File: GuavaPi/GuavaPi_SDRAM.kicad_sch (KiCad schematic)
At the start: 1 part

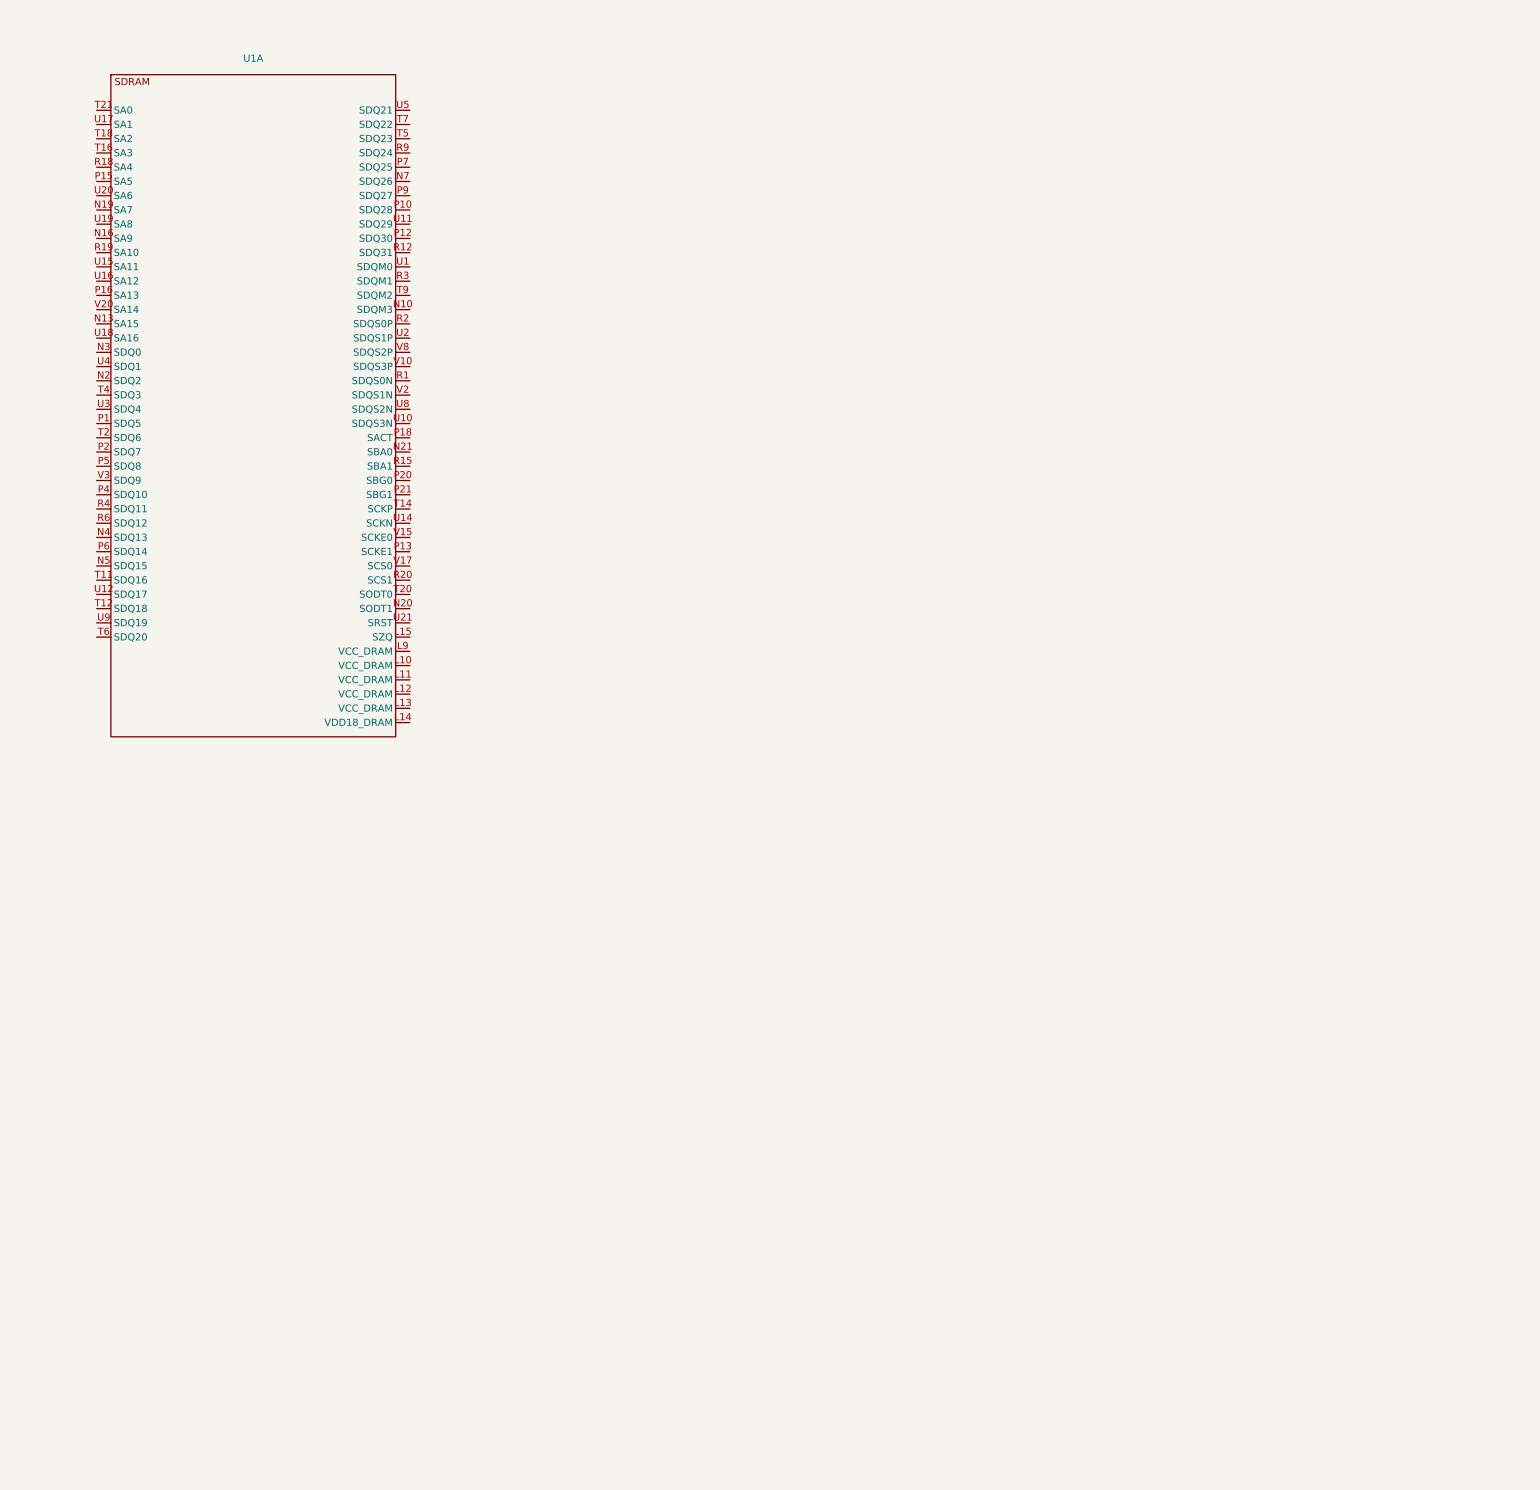
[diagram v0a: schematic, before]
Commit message: Started DRAM Design
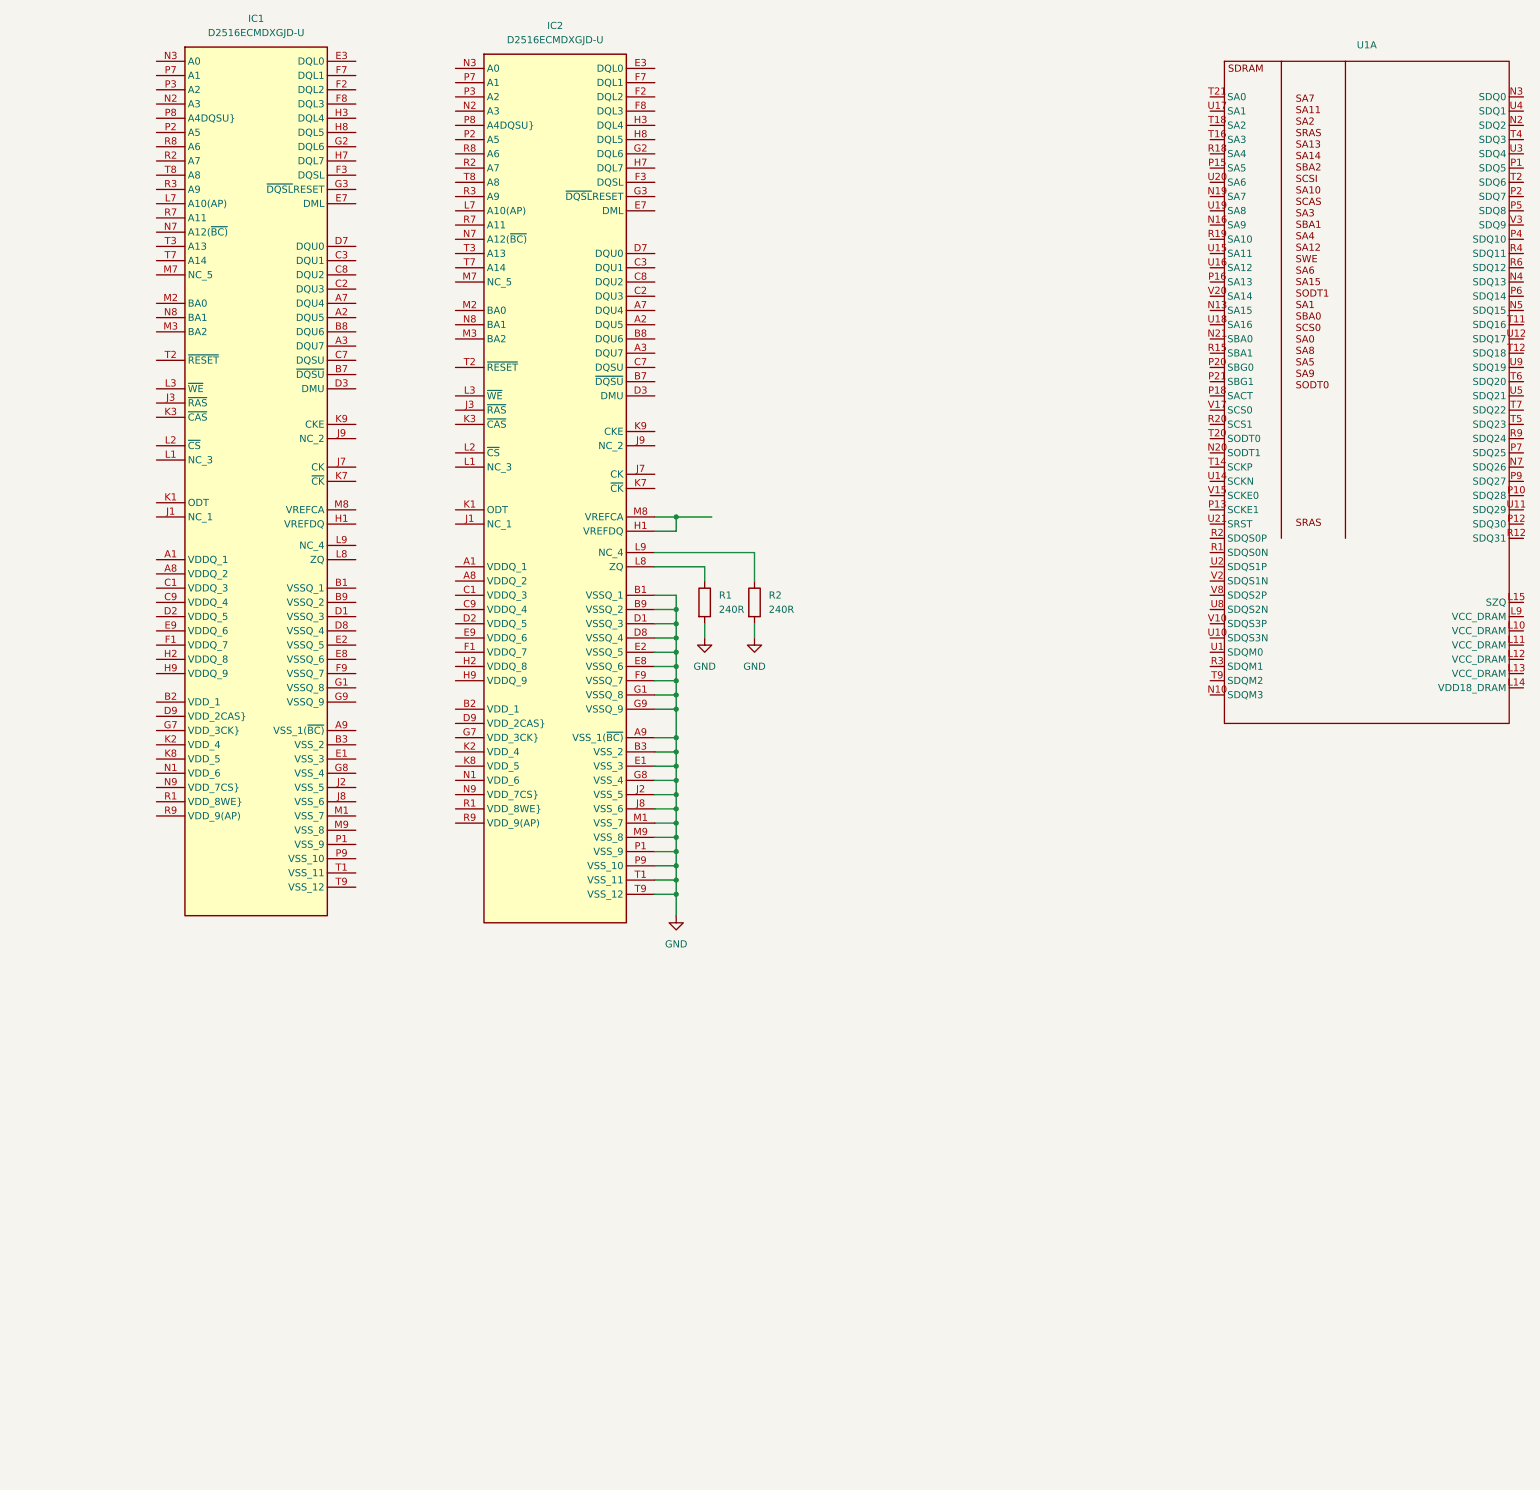
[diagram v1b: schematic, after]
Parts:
- added IC1, IC2: D2516ECMDXGJD-U, BGA96C80P9X16_750X1350X120, symbol D2516ECMDXGJD-U:D2516ECMDXGJD-U
- added R1, R2: 240R, symbol Device:R
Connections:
- new net: IC2.L8 (ZQ), R1.1
- new net: IC2.H1 (VREFDQ), IC2.M8 (VREFCA)
- new net: IC2.L9 (NC_4), R2.1
- new net GND: IC2.A9 (VSS_1(~{BC)}), IC2.B1 (VSSQ_1), IC2.B3 (VSS_2), IC2.B9 (VSSQ_2), IC2.D1 (VSSQ_3), IC2.D8 (VSSQ_4), IC2.E1 (VSS_3), IC2.E2 (VSSQ_5), IC2.E8 (VSSQ_6), IC2.F9 (VSSQ_7), IC2.G1 (VSSQ_8), IC2.G8 (VSS_4), IC2.G9 (VSSQ_9), IC2.J2 (VSS_5), IC2.J8 (VSS_6), IC2.M1 (VSS_7), IC2.M9 (VSS_8), IC2.P1 (VSS_9), IC2.P9 (VSS_10), IC2.T1 (VSS_11), IC2.T9 (VSS_12), R1.2, R2.2
